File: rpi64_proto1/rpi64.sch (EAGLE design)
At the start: 101 parts, among them Q1 BSS123, Q2 BSS123

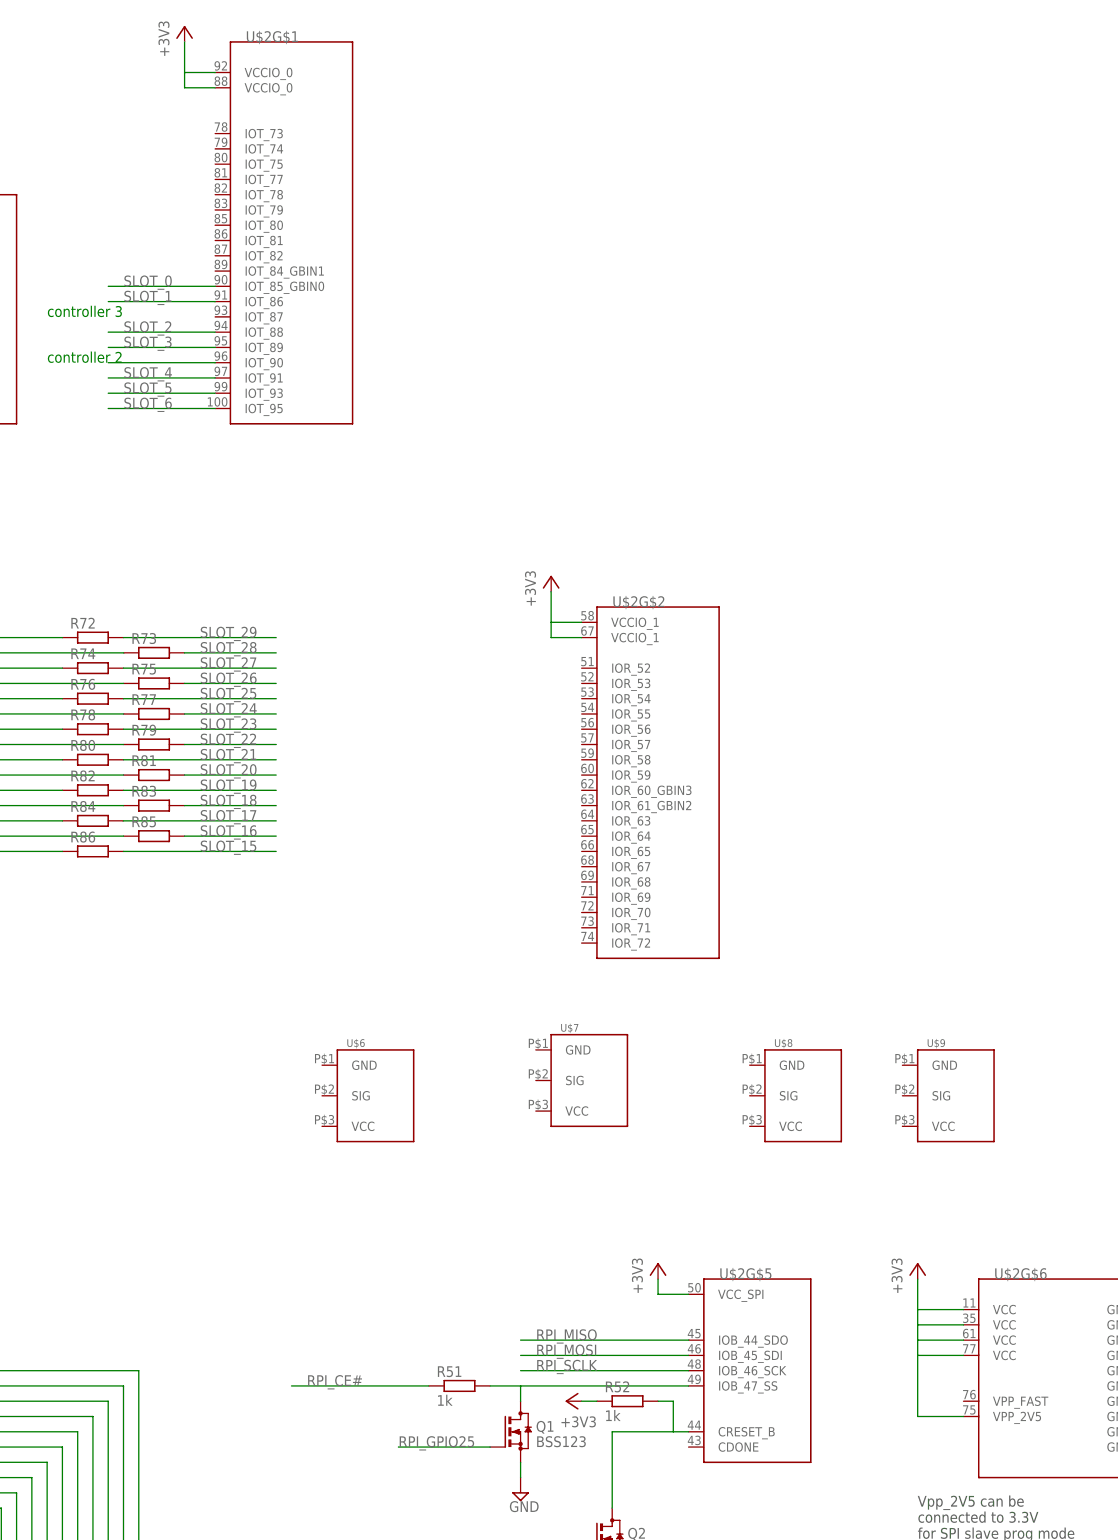
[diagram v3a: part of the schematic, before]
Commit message: Added decoupling capacitors
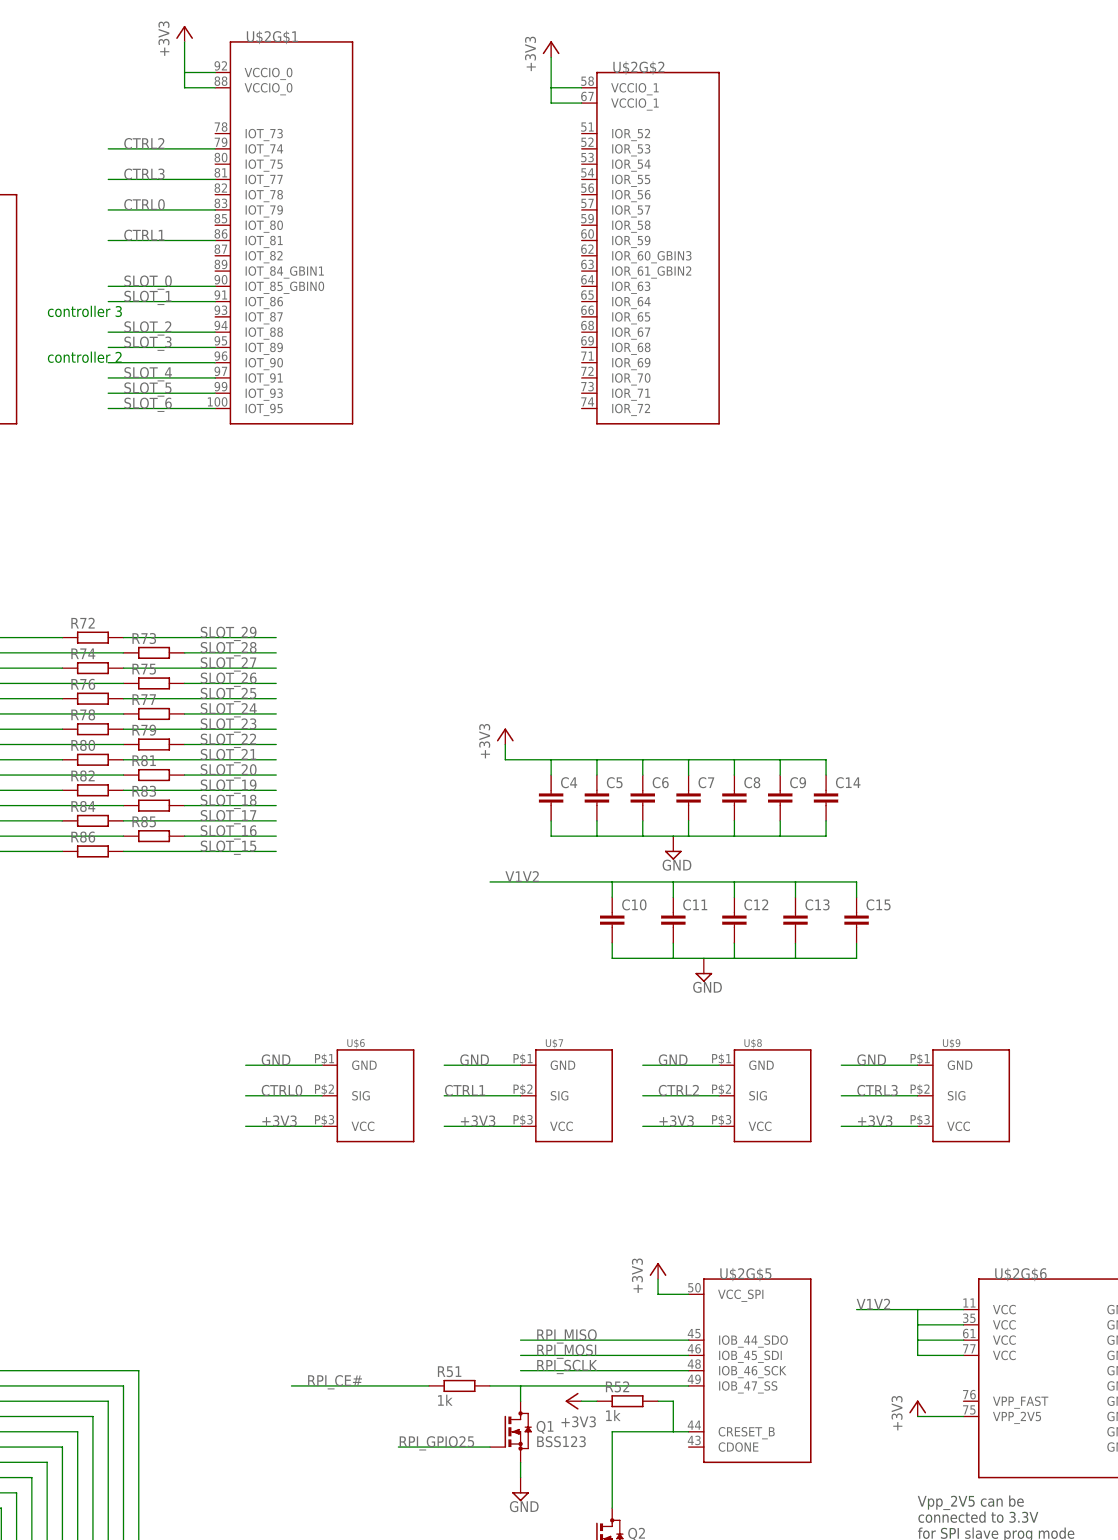
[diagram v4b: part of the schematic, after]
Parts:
- added C10, C11, C12, C13, C14, C15, C4, C5, C6, C7, C8, C9: (no value), rcl:C-EUC0805
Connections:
- new net CTRL0: U$2G$1.IOT_79, U$6.SIG
- new net CTRL1: U$2G$1.IOT_81, U$7.SIG
- new net CTRL2: U$2G$1.IOT_74, U$8.SIG
- new net CTRL3: U$2G$1.IOT_77, U$9.SIG
- net +3V3: now also C14.1, C4.1, C5.1, C6.1, C7.1, C8.1, C9.1, U$6.VCC, U$7.VCC, U$8.VCC, U$9.VCC; no longer U$2G$6.VCC, U$2G$6.VCC@1, U$2G$6.VCC@2, U$2G$6.VCC@3
- net GND: now also C10.2, C11.2, C12.2, C13.2, C14.2, C15.2, C4.2, C5.2, C6.2, C7.2, C8.2, C9.2, U$6.GND, U$7.GND, U$8.GND, U$9.GND
- net V1V2: now also C10.1, C11.1, C12.1, C13.1, C15.1, U$2G$6.VCC, U$2G$6.VCC@1, U$2G$6.VCC@2, U$2G$6.VCC@3
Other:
- moved on the sheet: U$2G$2, U$7, U$8, U$9

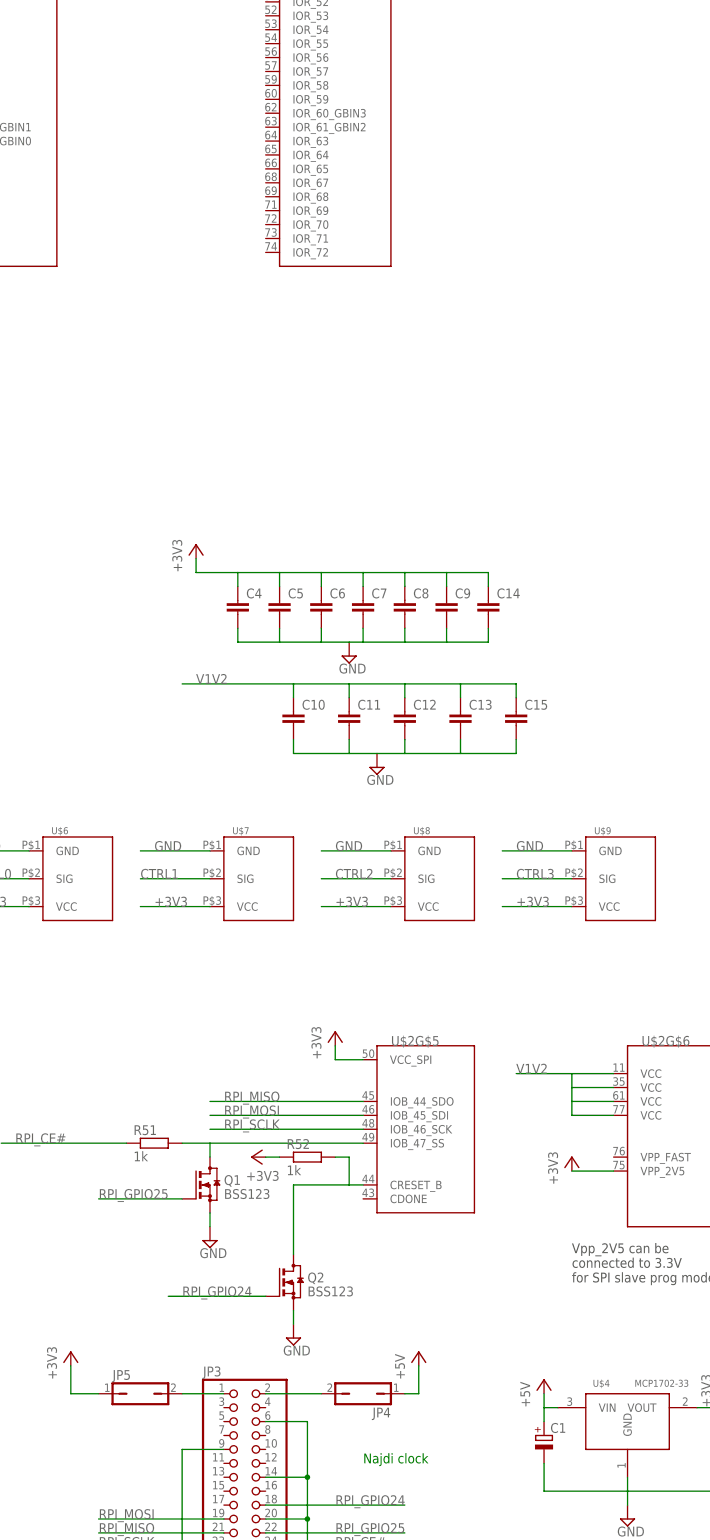
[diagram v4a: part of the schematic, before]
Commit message: Added clocks
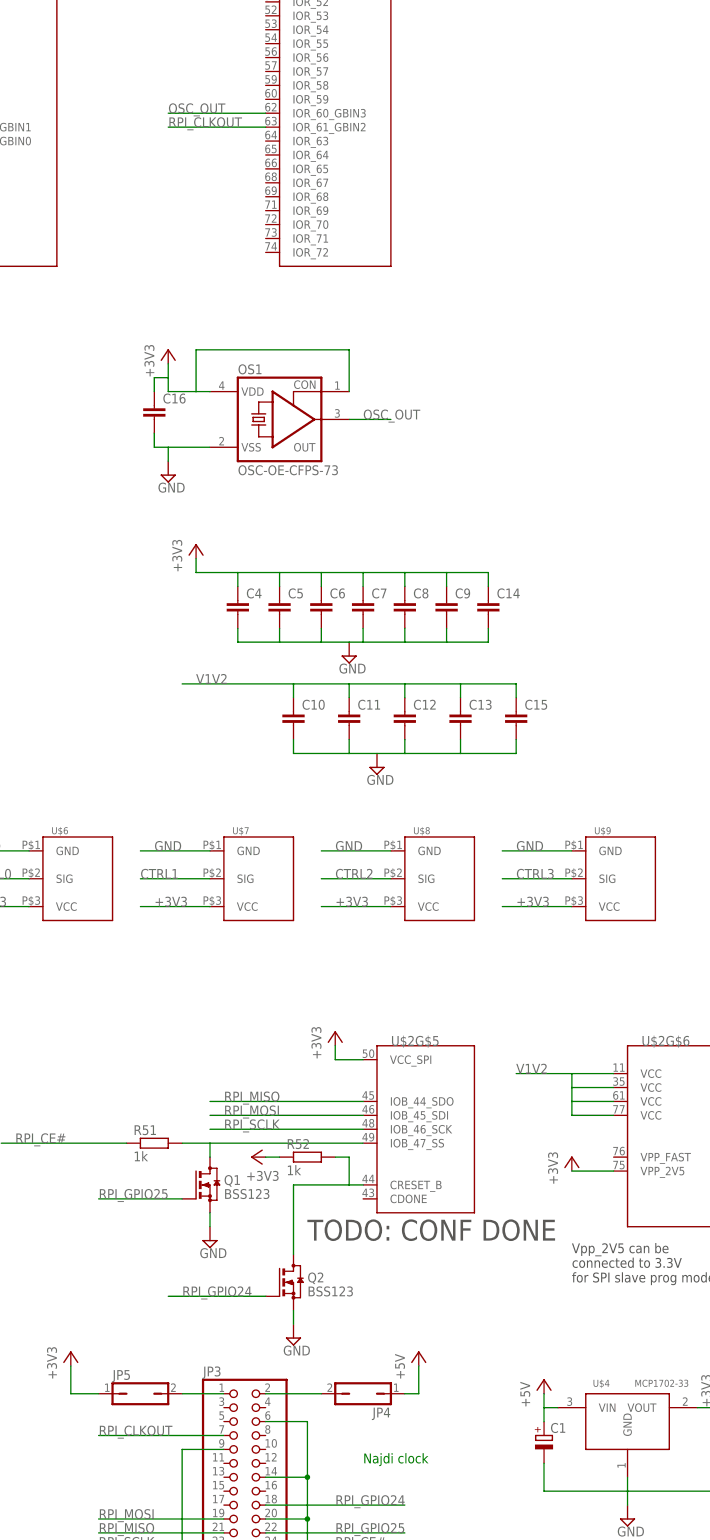
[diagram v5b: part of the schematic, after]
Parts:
- added C16: (no value), rcl:C-EUC0805
- added OS1: OSC-OE-CFPS-73, IQD-Frequency-Products:OSC-OE-CFPS-73
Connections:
- new net OSC_OUT: OS1.OUT, U$2G$2.IOR_60_GBIN3
- new net RPI_CLKOUT: JP3.7, U$2G$2.IOR_61_GBIN2
- net +3V3: now also C16.1, OS1.CON, OS1.VDD
- net GND: now also C16.2, OS1.VSS
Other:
- note added: "TODO: CONF DONE"
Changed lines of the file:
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@@
 <part name="C14" library="rcl" deviceset="C-EU" device="C0805"/>
 <part name="C15" library="rcl" deviceset="C-EU" device="C0805"/>
+<part name="OS1" library="IQD-Frequency-Products" deviceset="OSC-OE" device="-CFPS-73"/>
+<part name="+3V12" library="supply1" deviceset="+3V3" device=""/>
+<part name="C16" library="rcl" deviceset="C-EU" device="C0805"/>
+<part name="SUPPLY10" library="supply2" deviceset="GND" device=""/>
 </parts>
 <sheets>
@@
 <text x="203.2" y="271.78" size="1.778" layer="91">controller 3</text>
 <text x="203.2" y="264.16" size="1.778" layer="91">controller 2</text>
+<text x="299.72" y="76.2" size="3.81" layer="97">TODO: CONF DONE</text>
 </plain>
 <instances>
@@
 <instance part="C14" gate="G$1" x="332.74" y="193.04"/>
 <instance part="C15" gate="G$1" x="337.82" y="172.72"/>
+<instance part="OS1" gate="A" x="294.64" y="226.06"/>
+<instance part="+3V12" gate="G$1" x="274.32" y="238.76"/>
+<instance part="C16" gate="G$1" x="271.78" y="228.6"/>
+<instance part="SUPPLY10" gate="GND" x="274.32" y="215.9"/>
 </instances>
 <busses>
@@
 <wire x1="332.74" y1="185.42" x2="325.12" y2="185.42" width="0.1524" layer="91"/>
 </segment>
+<segment>
+<pinref part="C16" gate="G$1" pin="2"/>
+<wire x1="271.78" y1="223.52" x2="271.78" y2="220.98" width="0.1524" layer="91"/>
+<wire x1="271.78" y1="220.98" x2="274.32" y2="220.98" width="0.1524" layer="91"/>
+<pinref part="SUPPLY10" gate="GND" pin="GND"/>
+<wire x1="274.32" y1="220.98" x2="274.32" y2="218.44" width="0.1524" layer="91"/>
+<pinref part="OS1" gate="A" pin="VSS"/>
+<wire x1="281.94" y1="220.98" x2="274.32" y2="220.98" width="0.1524" layer="91"/>
+</segment>
 </net>
 <net name="N$102" class="0">
@@
 <wire x1="332.74" y1="198.12" x2="325.12" y2="198.12" width="0.1524" layer="91"/>
 </segment>
+<segment>
+<pinref part="+3V12" gate="G$1" pin="+3V3"/>
+<wire x1="274.32" y1="236.22" x2="274.32" y2="233.68" width="0.1524" layer="91"/>
+<wire x1="274.32" y1="233.68" x2="271.78" y2="233.68" width="0.1524" layer="91"/>
+<pinref part="C16" gate="G$1" pin="1"/>
+<wire x1="271.78" y1="233.68" x2="271.78" y2="231.14" width="0.1524" layer="91"/>
+<pinref part="OS1" gate="A" pin="VDD"/>
+<wire x1="281.94" y1="231.14" x2="279.4" y2="231.14" width="0.1524" layer="91"/>
+<wire x1="279.4" y1="231.14" x2="274.32" y2="231.14" width="0.1524" layer="91"/>
+<wire x1="274.32" y1="231.14" x2="274.32" y2="233.68" width="0.1524" layer="91"/>
+<pinref part="OS1" gate="A" pin="CON"/>
+<wire x1="307.34" y1="231.14" x2="307.34" y2="238.76" width="0.1524" layer="91"/>
+<wire x1="307.34" y1="238.76" x2="279.4" y2="238.76" width="0.1524" layer="91"/>
+<wire x1="279.4" y1="238.76" x2="279.4" y2="231.14" width="0.1524" layer="91"/>
+</segment>
 </net>
 <net name="+5V" class="0">
@@
 </segment>
 </net>
+<net name="RPI_CLKOUT" class="0">
+<segment>
+<pinref part="JP3" gate="A" pin="7"/>
+<wire x1="284.48" y1="40.64" x2="261.62" y2="40.64" width="0.1524" layer="91"/>
+<label x="261.62" y="40.64" size="1.778" layer="95"/>
+</segment>
+<segment>
+<pinref part="U$2" gate="G$2" pin="IOR_61_GBIN2"/>
+<wire x1="292.1" y1="279.4" x2="274.32" y2="279.4" width="0.1524" layer="91"/>
+<label x="274.32" y="279.4" size="1.778" layer="95"/>
+</segment>
+</net>
+<net name="OSC_OUT" class="0">
+<segment>
+<pinref part="U$2" gate="G$2" pin="IOR_60_GBIN3"/>
+<wire x1="292.1" y1="281.94" x2="274.32" y2="281.94" width="0.1524" layer="91"/>
+<label x="274.32" y="281.94" size="1.778" layer="95"/>
+</segment>
+<segment>
+<pinref part="OS1" gate="A" pin="OUT"/>
+<wire x1="307.34" y1="226.06" x2="314.96" y2="226.06" width="0.1524" layer="91"/>
+<label x="309.88" y="226.06" size="1.778" layer="95"/>
+</segment>
+</net>
